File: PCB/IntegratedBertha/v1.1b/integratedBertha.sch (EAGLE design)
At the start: 99 parts, among them CON1 SPI, IC1 REG1117, IC2 AD8223, J1 RJ12, J2 RJ12, J3 RJ12, J4 RJ12, J5 RJ12, J7 22--02, Q1 BSP75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

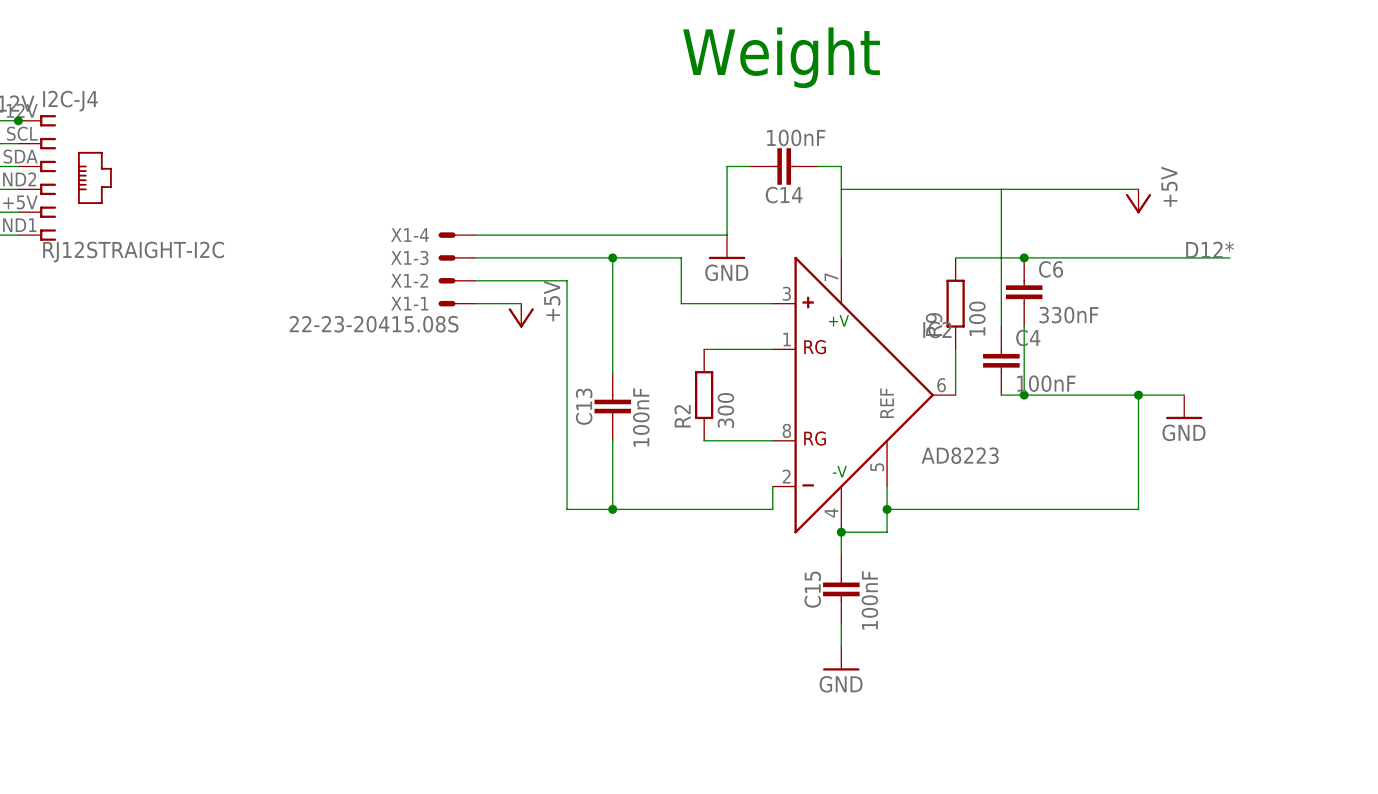
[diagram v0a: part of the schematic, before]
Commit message: added RF filter capacitances. autorouter works still 100percent
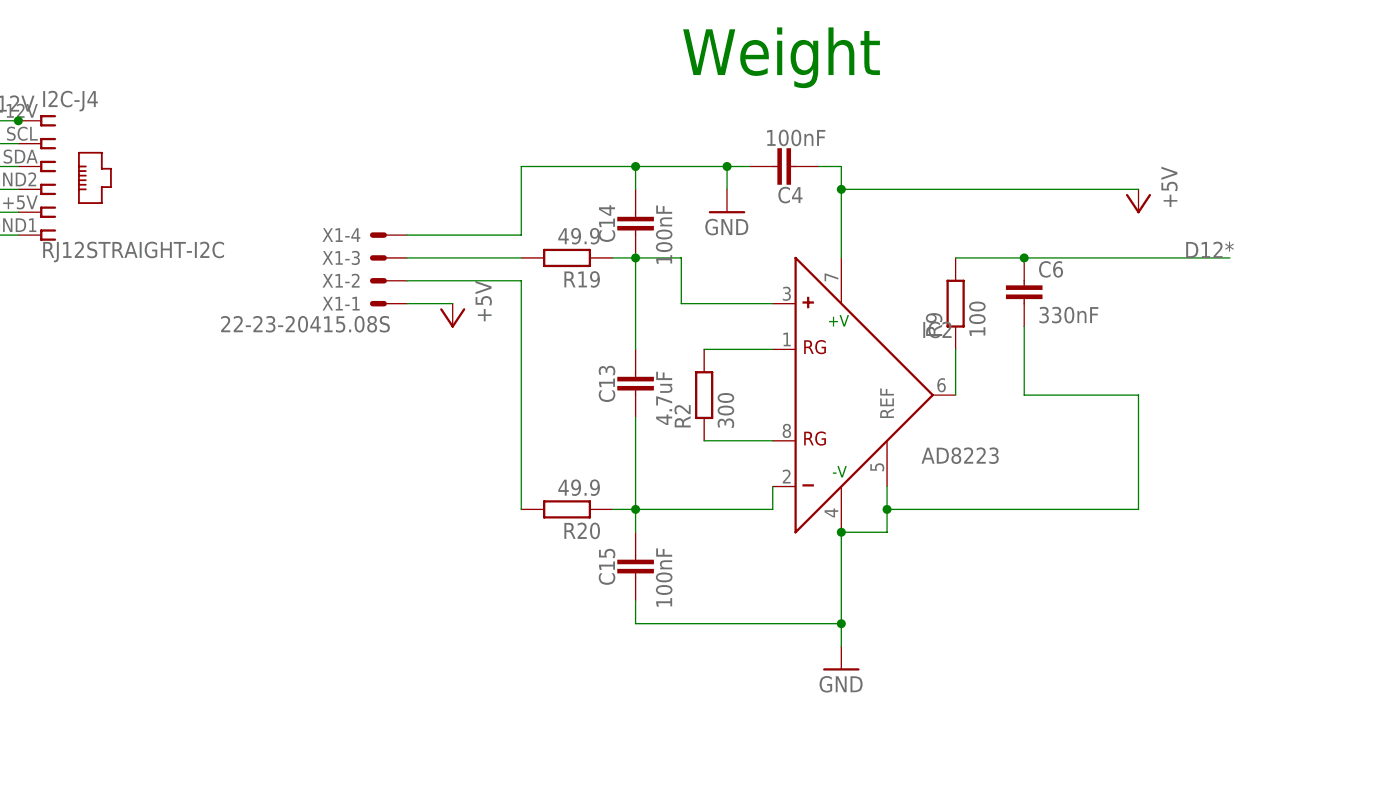
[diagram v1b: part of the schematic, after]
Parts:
- added R19, R20: 49.9, resistor:R-EU_R1206
- C13: value 100nF -> 4.7uF
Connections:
- new net N$31: R20.2, X1-2.S
- new net N$37: R19.2, X1-3.S
- net +5V: now also C4.2; no longer C14.2, C4.1
- net DIFF+: now also C14.2, R19.1; no longer X1-3.S
- net DIFF-: now also C15.1, R20.1; no longer X1-2.S
- net GND: now also C4.1; no longer C15.1, C4.2
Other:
- moved on the sheet: C13, C14, C15, C4, X1-1, X1-2, X1-3, X1-4

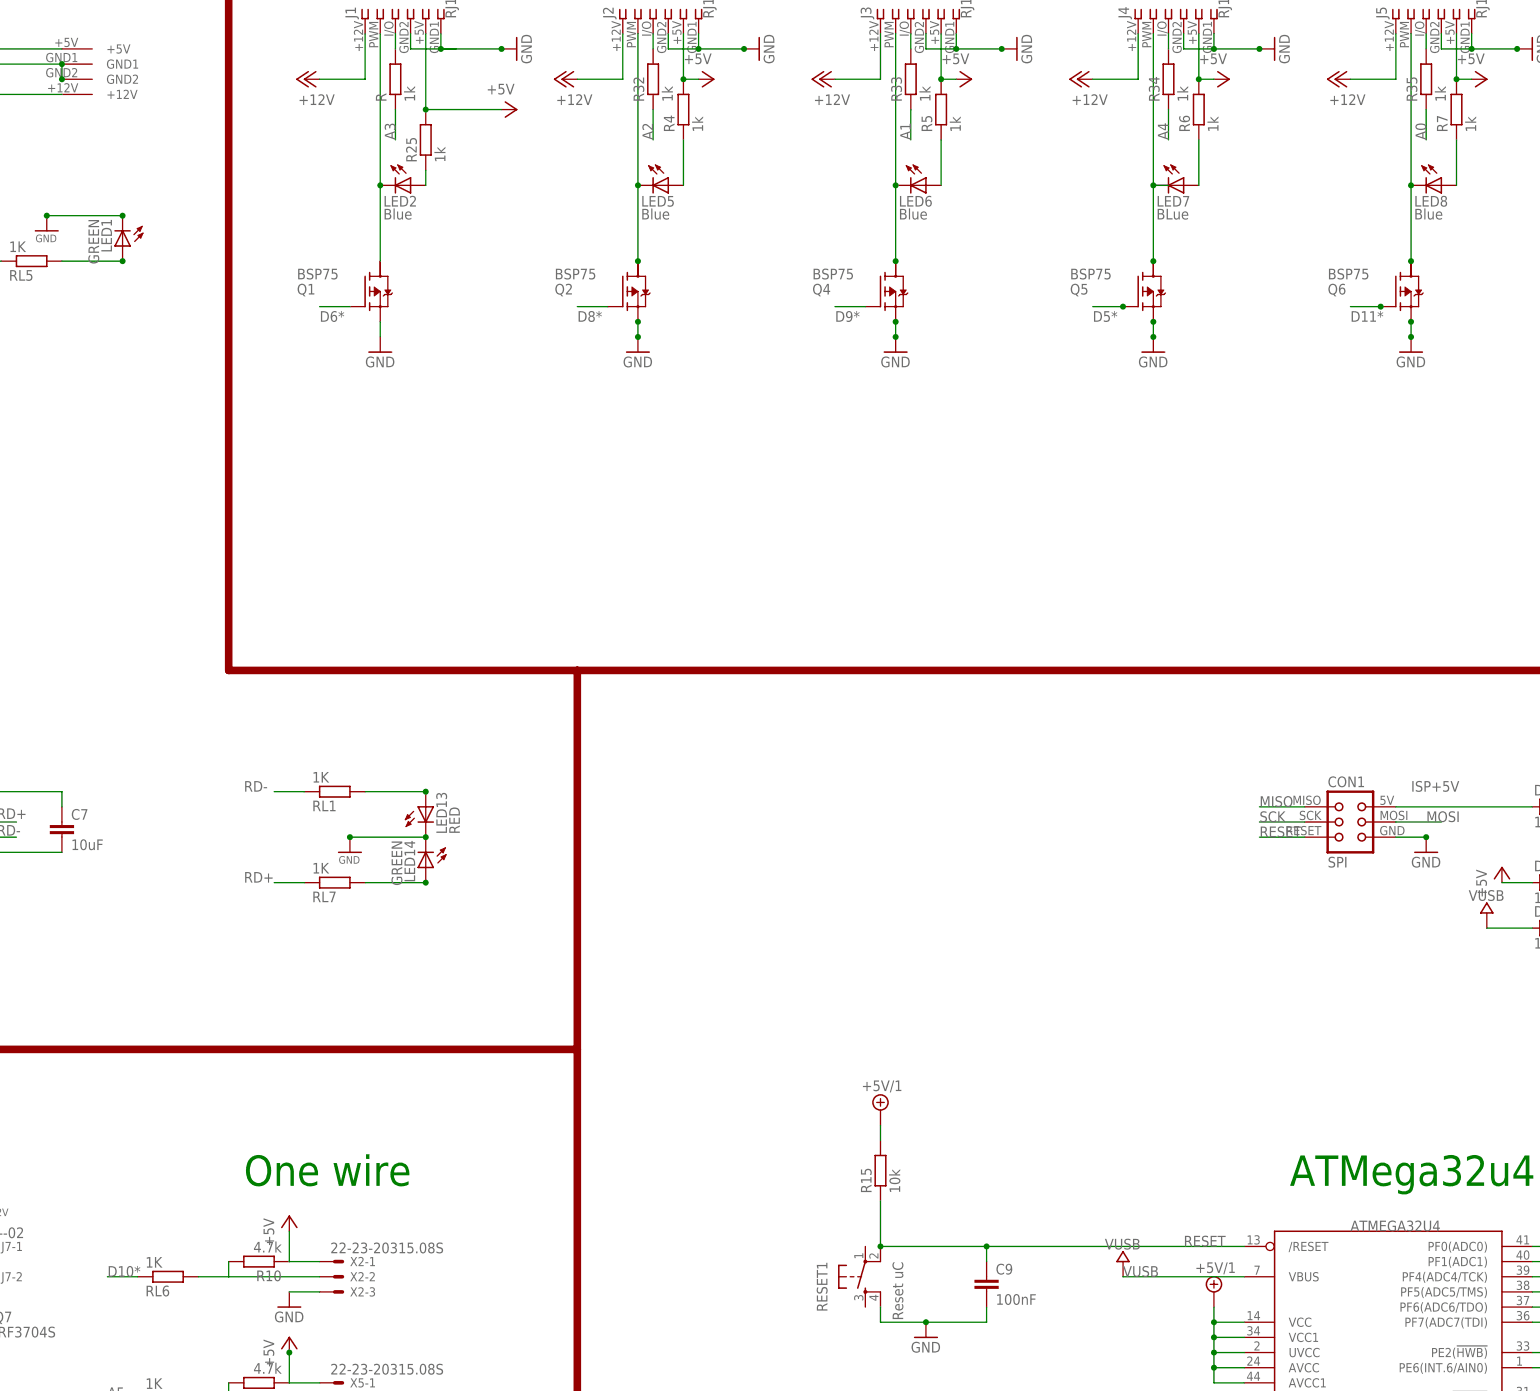
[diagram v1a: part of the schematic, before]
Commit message: modified pin configuration to newest version as in googledocs
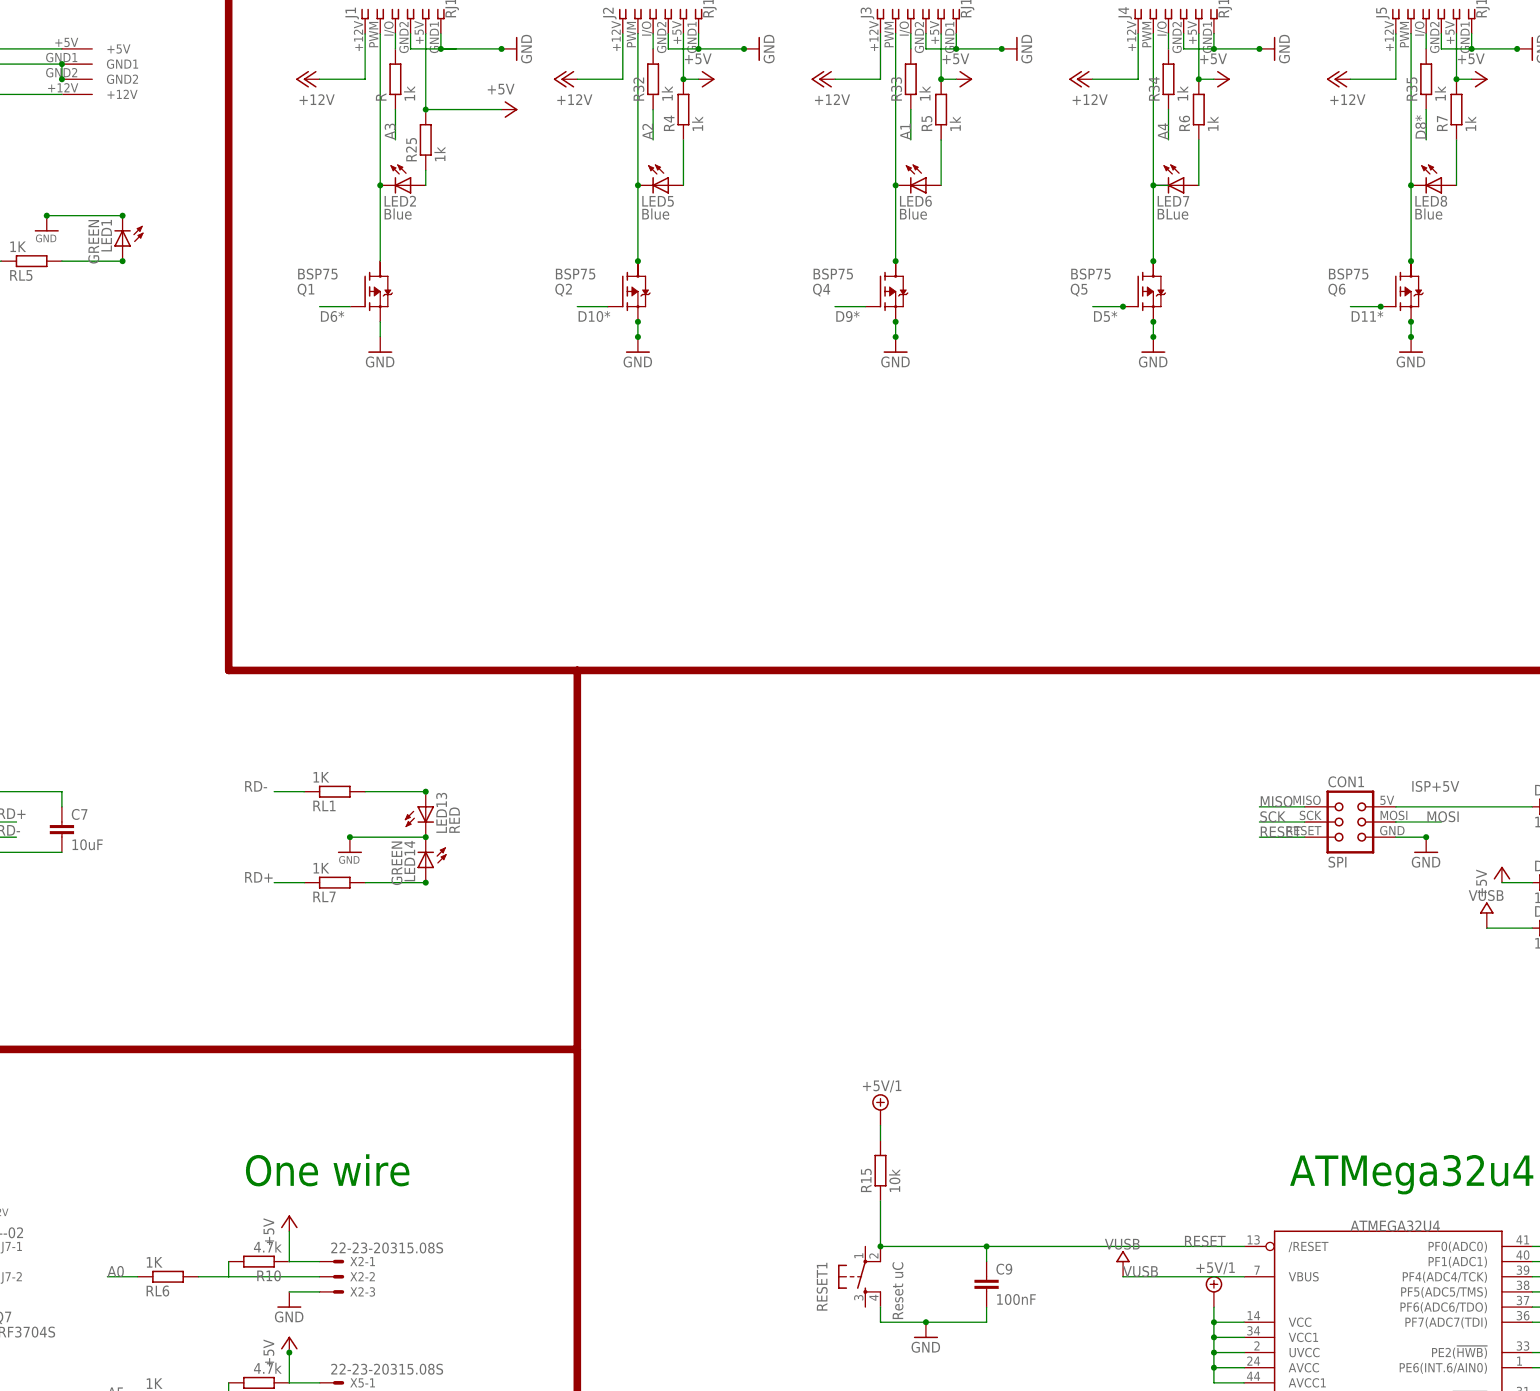
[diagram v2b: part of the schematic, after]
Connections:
- net A0: now also RL6.1; no longer R35.1
- net D10*: now also Q2.G; no longer RL6.1
- net D8*: now also R35.1; no longer Q2.G
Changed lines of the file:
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@@
 </segment>
 <segment>
-<pinref part="RL6" gate="G$1" pin="1"/>
-<wire x1="12.7" y1="83.82" x2="7.62" y2="83.82" width="0.1524" layer="91"/>
-<label x="7.62" y="83.82" size="1.778" layer="95"/>
+<pinref part="Q2" gate="G$1" pin="G"/>
+<wire x1="91.44" y1="246.38" x2="86.36" y2="246.38" width="0.1524" layer="91"/>
+<label x="86.36" y="243.84" size="1.778" layer="95"/>
 </segment>
 </net>
@@
 </segment>
 <segment>
-<pinref part="R35" gate="G$1" pin="1"/>
-<wire x1="228.6" y1="279.4" x2="228.6" y2="274.32" width="0.1524" layer="91"/>
-<label x="228.6" y="274.32" size="1.778" layer="95" rot="R90"/>
+<pinref part="RL6" gate="G$1" pin="1"/>
+<wire x1="12.7" y1="83.82" x2="7.62" y2="83.82" width="0.1524" layer="91"/>
+<label x="7.62" y="83.82" size="1.778" layer="95"/>
 </segment>
 </net>
@@
 </segment>
 <segment>
-<pinref part="Q2" gate="G$1" pin="G"/>
-<wire x1="91.44" y1="246.38" x2="86.36" y2="246.38" width="0.1524" layer="91"/>
-<label x="86.36" y="243.84" size="1.778" layer="95"/>
-</segment>
-</net>
+<pinref part="R35" gate="G$1" pin="1"/>
+<wire x1="228.6" y1="279.4" x2="228.6" y2="274.32" width="0.1524" layer="91"/>
+<label x="228.6" y="274.32" size="1.778" layer="95" rot="R90"/>
+</segment>
+</net>
